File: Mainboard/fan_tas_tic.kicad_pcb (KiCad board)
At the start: 2 copper layers, 155 x 175 mm, 123 parts, among them J1 Ti_Booster_40, P1 CONN_01X04, P10 CONN_01X08, P11 CONN_01X04, P12 CONN_01X04, P13 CONN_01X04, P14 CONN_01X04, P2 CONN_01X04, P3 CONN_01X04, P4 CONN_01X04, P5 CONN_01X04, P6 CONN_01X08, P7 CONN_01X08, P8 CONN_01X08, P9 CONN_01X08, Q1 IRL640, Q10 IRL640, Q11 IRL640, Q12 IRL640, Q13 BSS138, Q14 BSS138, Q15 BSS138, Q16 BSS138, Q17 BSS138, Q18 BSS138, Q19 BSS138, Q2 IRL640, Q20 BSS138, Q3 IRL640, Q4 IRL640, Q5 IRL640, Q6 IRL640, Q7 IRL640, Q8 IRL640, Q9 IRL640, U1 7812, U2 7805, U3 UCC27524, U4 UCC27524, U5 TPIC6B595, U6 PCF8574, U7 74HC04

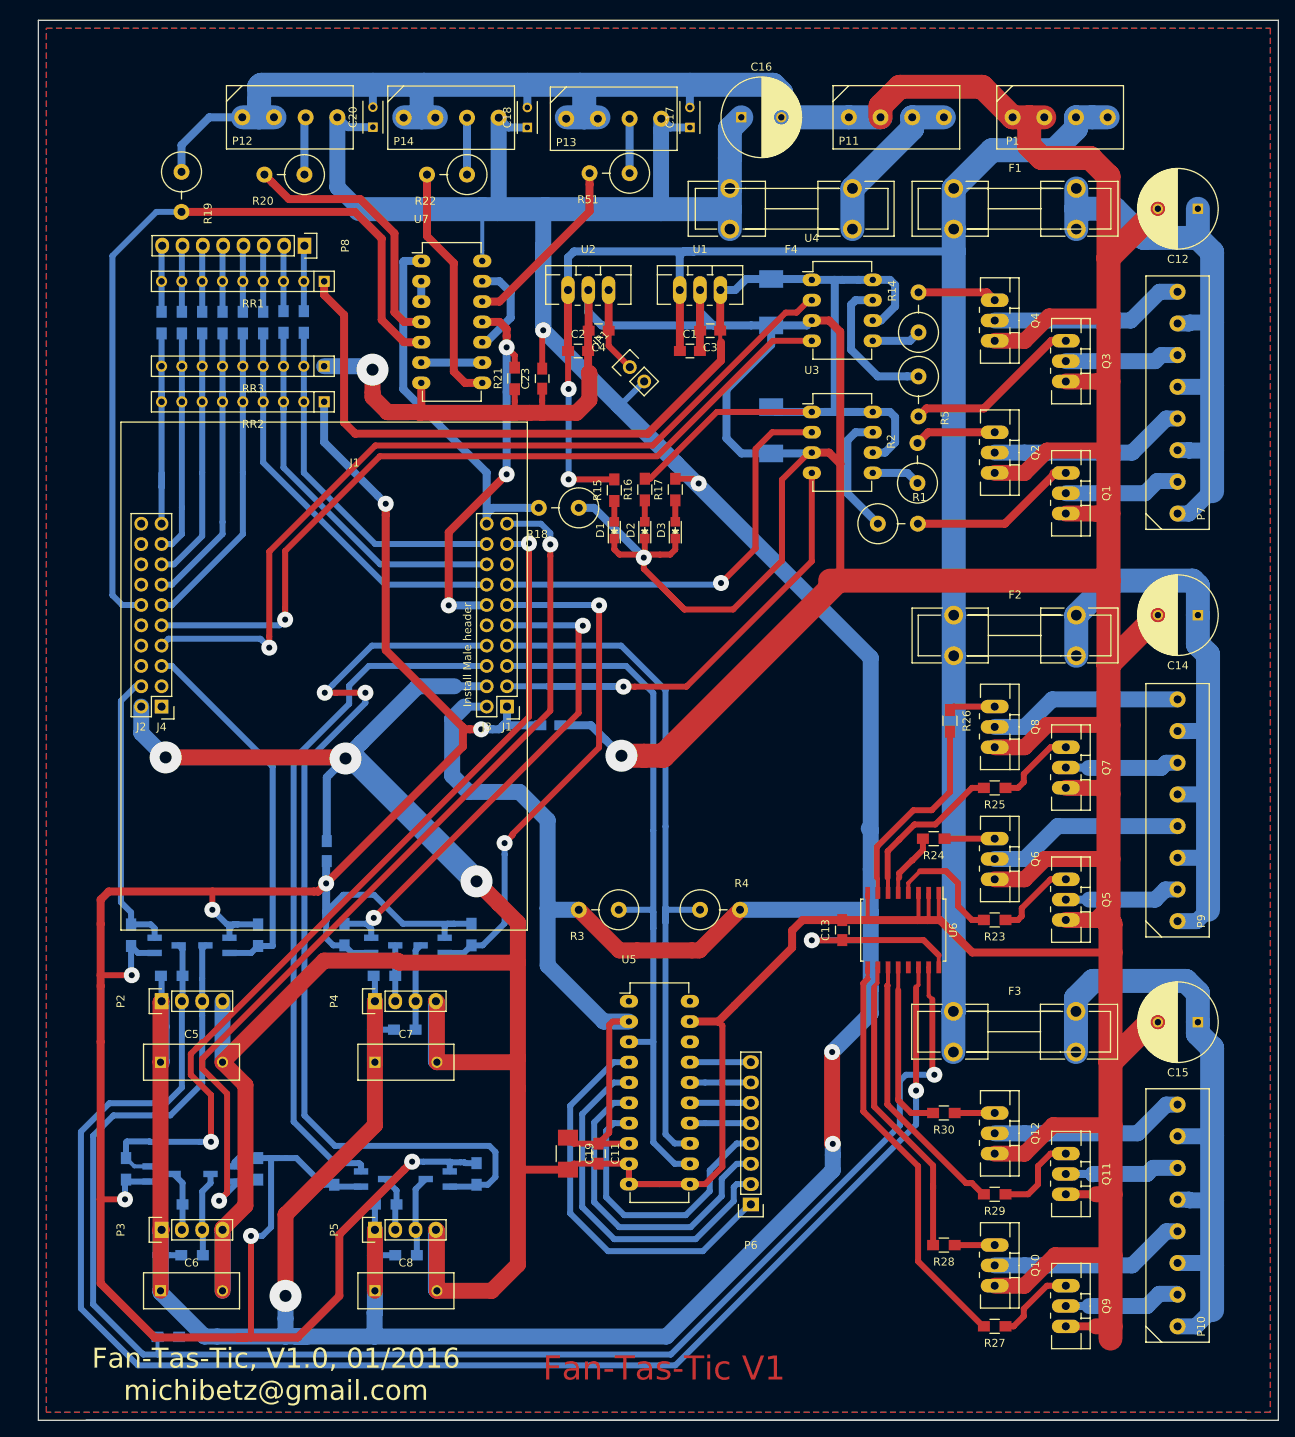
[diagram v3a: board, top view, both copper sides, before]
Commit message: Separated Tiva 5V from Power 5 V
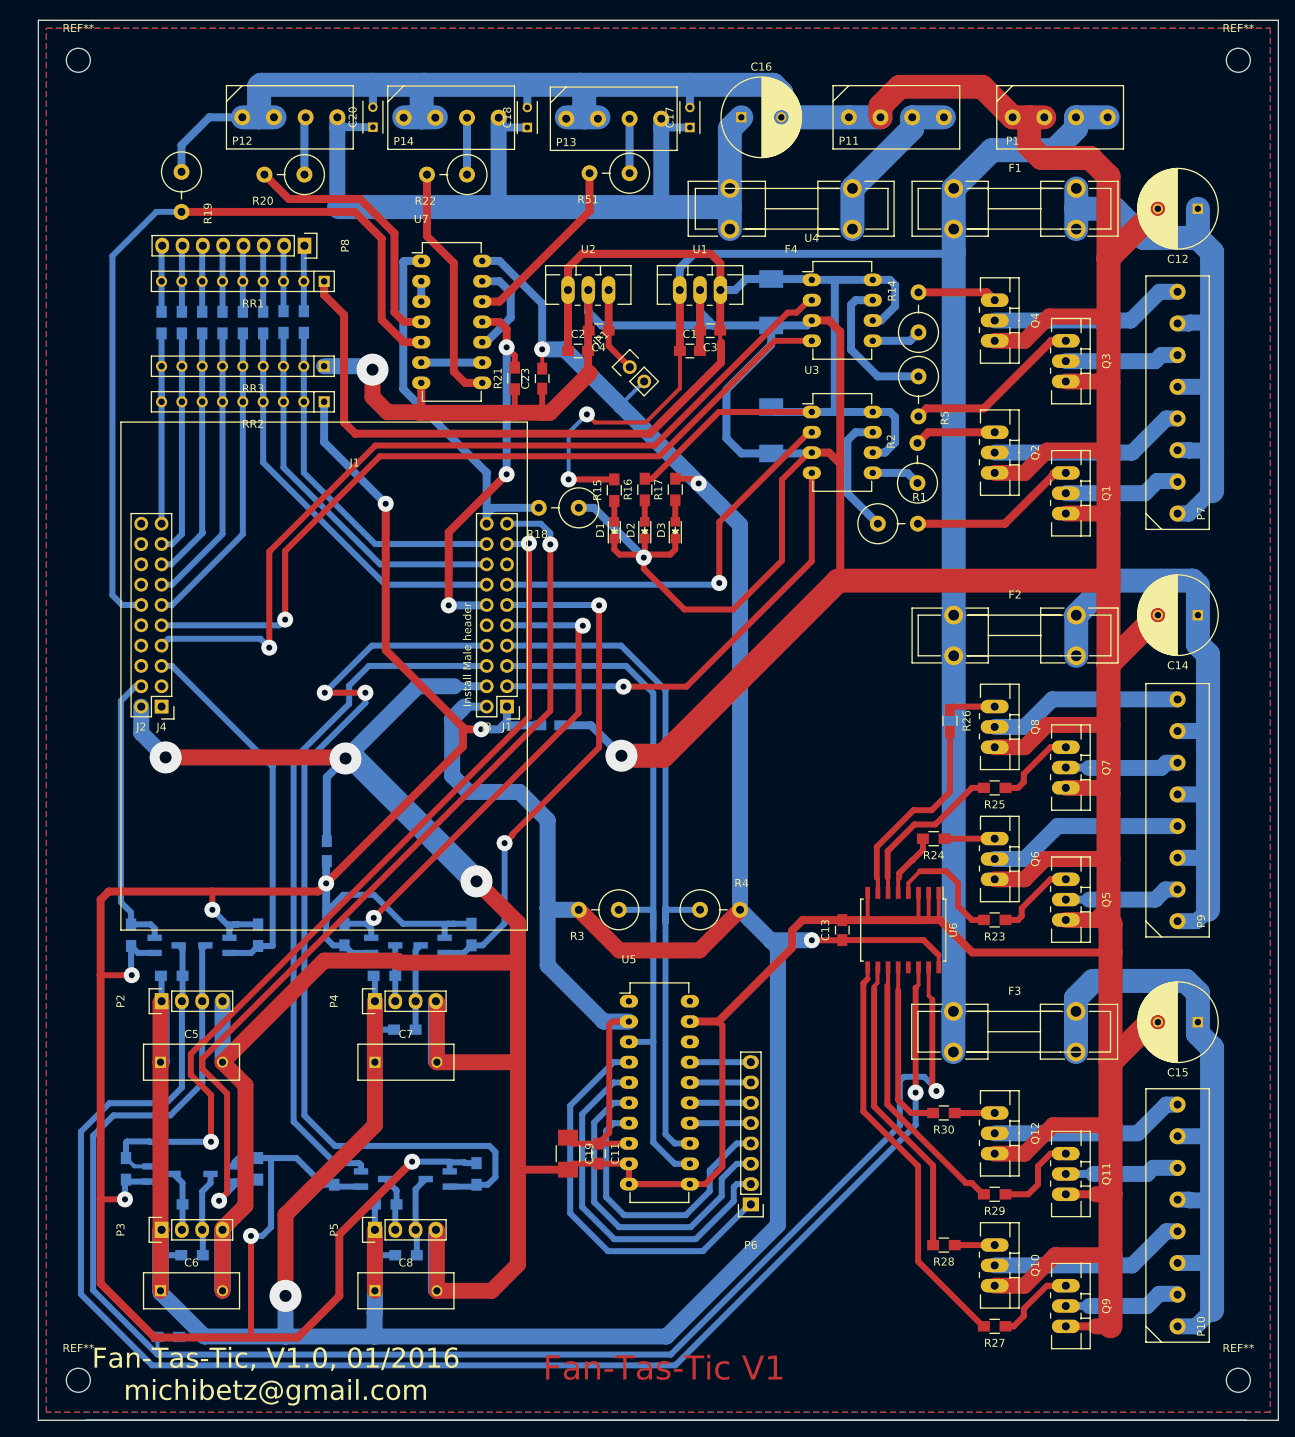
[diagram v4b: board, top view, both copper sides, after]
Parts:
- added REF**: MountingHole_3mm, Mounting_Holes:MountingHole_3mm, F.Cu at (20.0, 185.0)
- added REF**: MountingHole_3mm, Mounting_Holes:MountingHole_3mm, F.Cu at (165.0, 185.0)
- added REF**: MountingHole_3mm, Mounting_Holes:MountingHole_3mm, F.Cu at (165.0, 20.0)
- added REF**: MountingHole_3mm, Mounting_Holes:MountingHole_3mm, F.Cu at (20.0, 20.0)
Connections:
- C16 pad 1: +5V -> +5VP
- C17 pad 1: +5V -> +5VP
- C18 pad 1: +5V -> +5VP
- C2 pad 1: +24V -> +12V
- C20 pad 1: +5V -> +5VP
- F4 pad 2: +5V -> +5VP
- P12 pad 4: +5V -> +5VP
- P13 pad 4: +5V -> +5VP
- P14 pad 4: +5V -> +5VP
- U2 pad VI: +24V -> +12V
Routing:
- net +5V: track 697.0 -> 521.4 mm, vias 6 -> 4
- net +5VP: track 0.00 -> 108.7 mm
- net +12V: track 175.4 -> 207.0 mm
- net +24V: track 227.7 -> 210.5 mm
- net GND: track 1197.9 -> 1185.4 mm
- net /TiviaBoard/po_3_pwm: track 65.2 -> 55.7 mm
- net /TiviaBoard/po_2_pwm: track 53.3 -> 50.5 mm
- net /powerChannel10/DRAIN: track 16.7 -> 14.3 mm
- net +3V3: track 343.0 -> 340.9 mm
- net /TiviaBoard/sm_row_7: track 28.1 -> 26.3 mm
- net /I2C_LEVEL_SHIFT0/B_5V: track 196.9 -> 198.6 mm
- net /TiviaBoard/sm_row_5: track 33.2 -> 31.8 mm
- net /I2C_LEVEL_SHIFT1/A_3V3: track 113.3 -> 112.2 mm
- net /I2C_LEVEL_SHIFT0/A_5V: track 194.8 -> 193.8 mm
- net /TiviaBoard/sm_row_1: track 48.5 -> 47.5 mm

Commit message: Larger pads and vias to allow some alignment error
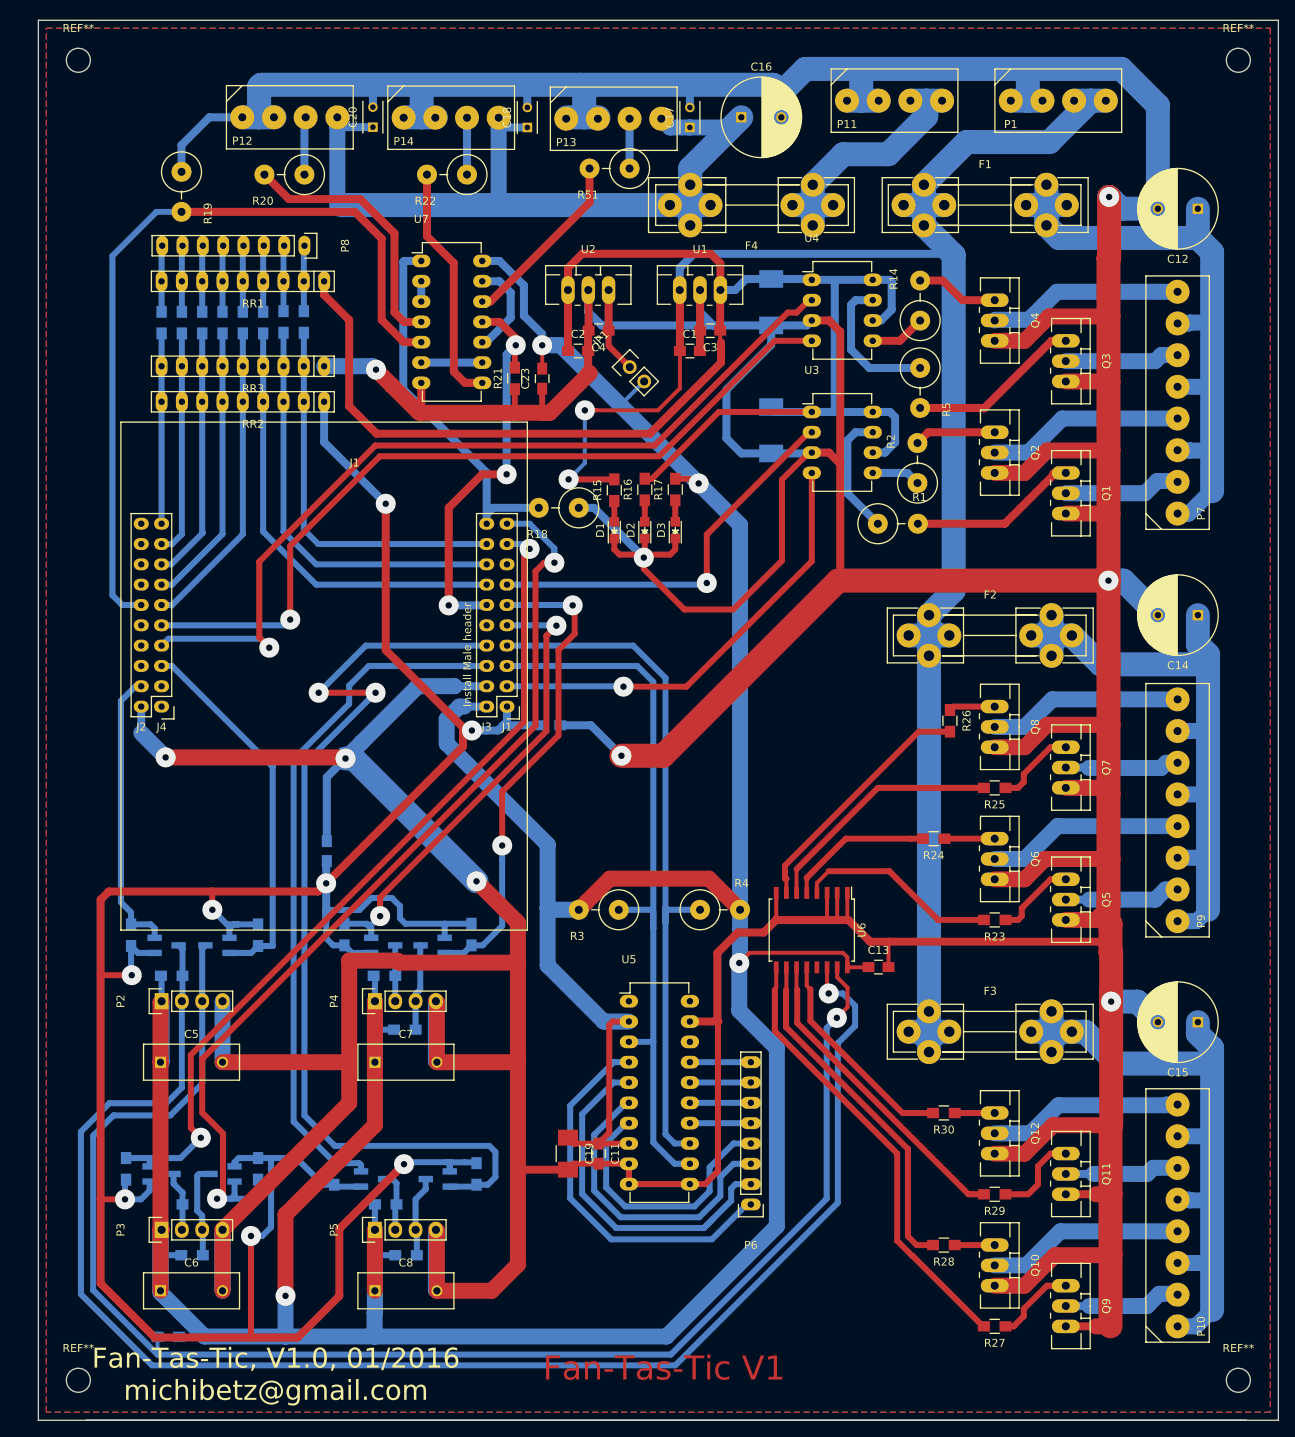
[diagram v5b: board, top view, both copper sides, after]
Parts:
- F1, F2, F3, F4: footprint Fuse_Holders_and_Fuses:Fuseholder5x20_horiz_open_lateral_Type-II -> Fuse_Holders_and_Fuses:Fuseholder5x20_horiz_open_universal_Type-III
- moved U6 11.4 mm to (111.7, 128.7)
- moved C13 6.47 mm to (120.0, 133.3), turned to 0 degrees
- moved F4 4.98 mm to (104.1, 38.1)
- moved F1 3.76 mm to (133.3, 38.1)
- moved F2 3.09 mm to (134.0, 91.9)
- moved F3 3.05 mm to (134.0, 141.4)
- moved P11 2.09 mm to (116.1, 29.0)
- moved P1 2.09 mm to (136.6, 29.0)
- moved R14 1.49 mm to (125.2, 50.0)
- moved R5 1.07 mm to (125.2, 61.0)
- moved R51 0.59 mm to (86.4, 33.5)
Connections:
- J1 pad 13: (no net) -> Net-(J1-Pad13)
- J1 pad 14: (no net) -> Net-(J1-Pad14)
- J1 pad 15: (no net) -> Net-(J1-Pad15)
- J1 pad 17: (no net) -> Net-(J1-Pad17)
- J1 pad 18: (no net) -> /TiviaBoard/SSI_0_RX
- J1 pad 19: (no net) -> /TiviaBoard/SSI_0_/SS
- J1 pad 20: (no net) -> /TiviaBoard/SSI_0_CLK
- J1 pad 25: (no net) -> Net-(J1-Pad25)
- J1 pad 31: (no net) -> Net-(J1-Pad31)
- J1 pad 32: (no net) -> Net-(J1-Pad32)
- J1 pad 8: (no net) -> /TiviaBoard/SSI_0_TX
- U5 pad 1: (no net) -> Net-(U5-Pad1)
- U5 pad 18: (no net) -> Net-(U5-Pad18)
- U5 pad 20: (no net) -> Net-(U5-Pad20)
- U6 pad 13: (no net) -> Net-(U6-Pad13)
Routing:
- net +24V: track 210.5 -> 247.8 mm
- net GND: track 1185.4 -> 1222.4 mm, vias 6 -> 9
- net Net-(F4-Pad1): track 21.0 -> 39.0 mm
- net Net-(C12-Pad1): track 76.4 -> 86.9 mm
- net /powerChannel5/CTRL: track 8.19 -> 18.6 mm
- net /powerChannel6/CTRL: track 20.5 -> 30.6 mm
- net /powerChannel4/CTRL: track 15.5 -> 25.3 mm
- net /I2C_LEVEL_SHIFT0/B_5V: track 198.6 -> 189.1 mm
- net +5V: track 521.4 -> 512.6 mm
- net Net-(C14-Pad1): track 101.7 -> 107.9 mm
- net /I2C_LEVEL_SHIFT1/A_3V3: track 112.2 -> 106.2 mm
- net /powerChannel7/CTRL: track 25.3 -> 31.2 mm
- net Net-(C15-Pad1): track 82.2 -> 88.0 mm
- net /powerChannel9/CTRL: track 38.0 -> 43.6 mm
- net /powerChannel10/CTRL: track 33.9 -> 39.5 mm
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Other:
- net class Default: via_dia 2 -> 2.5; via_drill 0.75 -> 0.8
- net class Power: via_dia 2 -> 2.5; via_drill 0.75 -> 0.8
- rule via_min_drill: 0.75 -> 0.8
- rule via_min_size: 2 -> 2.5

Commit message: Cleaned up traces
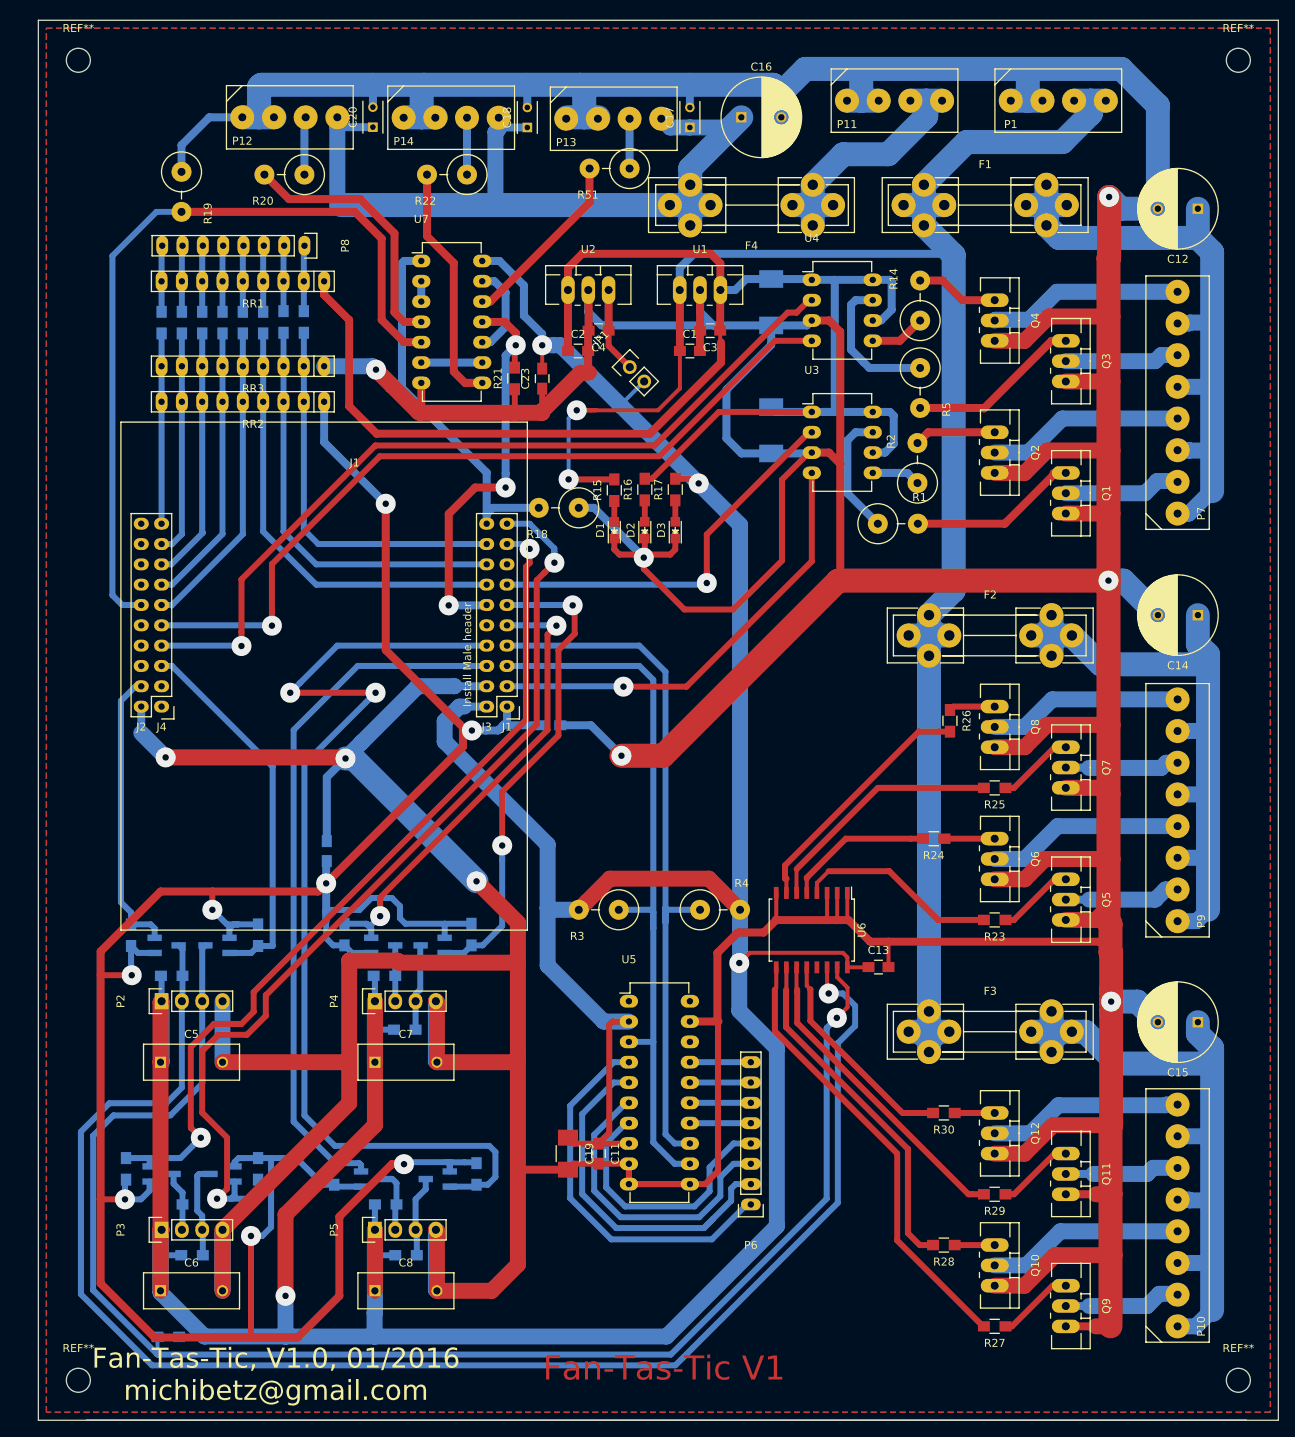
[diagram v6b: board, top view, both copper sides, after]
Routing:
- net /I2C_LEVEL_SHIFT3/B_3V3: track 122.2 -> 129.3 mm
- net /TiviaBoard/po_6_pwm: track 108.2 -> 104.1 mm
- net +24V: track 247.8 -> 251.7 mm
- net +3V3: track 344.1 -> 341.2 mm
- net /I2C_LEVEL_SHIFT1/A_3V3: track 106.2 -> 108.2 mm
- net /I2C_LEVEL_SHIFT1/B_3V3: track 118.2 -> 119.9 mm
- net Net-(Q11-Pad1): track 11.0 -> 9.64 mm
- net /TiviaBoard/SSI_3_TX: track 51.3 -> 52.1 mm
- net /I2C_LEVEL_SHIFT3/A_3V3: track 87.1 -> 87.9 mm
- net /TiviaBoard/po_7_pwm: track 101.4 -> 100.8 mm
- net Net-(U7-Pad10): track 12.1 -> 11.5 mm
- net Net-(Q5-Pad1): track 10.2 -> 9.64 mm
- net Net-(Q7-Pad1): track 10.2 -> 9.64 mm
- net Net-(Q9-Pad1): track 10.2 -> 9.64 mm
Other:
- board text added: "01/2016"
- board text added: "1.0"
- board text added: "Fan-Tas-tic Pinball controller"
- board text added: "Mainboard"
- board text added: "Pinball controller based on TM4C123G LaunchPad eval. kit. Features: 8x8 Switch matrix inputs, 12 onboard drivers for solenoids, 4 of them can do hardware PWM (> 100 kHz), 4 x I2C channels for extension boards, 3 x SPI channels for running WS2811 / WS2812 LED strings with up to 1024 LEDs per channel, In- / Outputs can be easily and cheaply added with PCF8574 I2C GPIO extenders"
- board text added: "michibetz@gmail.com"

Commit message: Small documentation updates
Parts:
- moved RR1 1.26 mm to (40.6, 48.9)
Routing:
- net +5V: track 512.9 -> 523.8 mm
- net /I2C_LEVEL_SHIFT2/B_3V3: track 60.7 -> 68.7 mm
- net /I2C_LEVEL_SHIFT1/B_3V3: track 119.9 -> 126.7 mm
- net /I2C_LEVEL_SHIFT2/A_3V3: track 58.7 -> 65.3 mm
- net /I2C_LEVEL_SHIFT1/A_3V3: track 108.2 -> 114.3 mm
- net /TiviaBoard/SSI_3_TX: track 52.1 -> 56.0 mm
- net +3V3: track 341.2 -> 343.7 mm
- net +12V: track 204.9 -> 203.4 mm
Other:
- board text added: "1.1"
- board text removed: "1.0"
